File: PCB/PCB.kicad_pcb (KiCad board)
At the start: 4 copper layers, 56 x 55 mm, 15 parts, among them P1 SEN-11574, U1 TinyS3_Symbol, U2 ADXL345, U3 ST7789V, U4 switch3

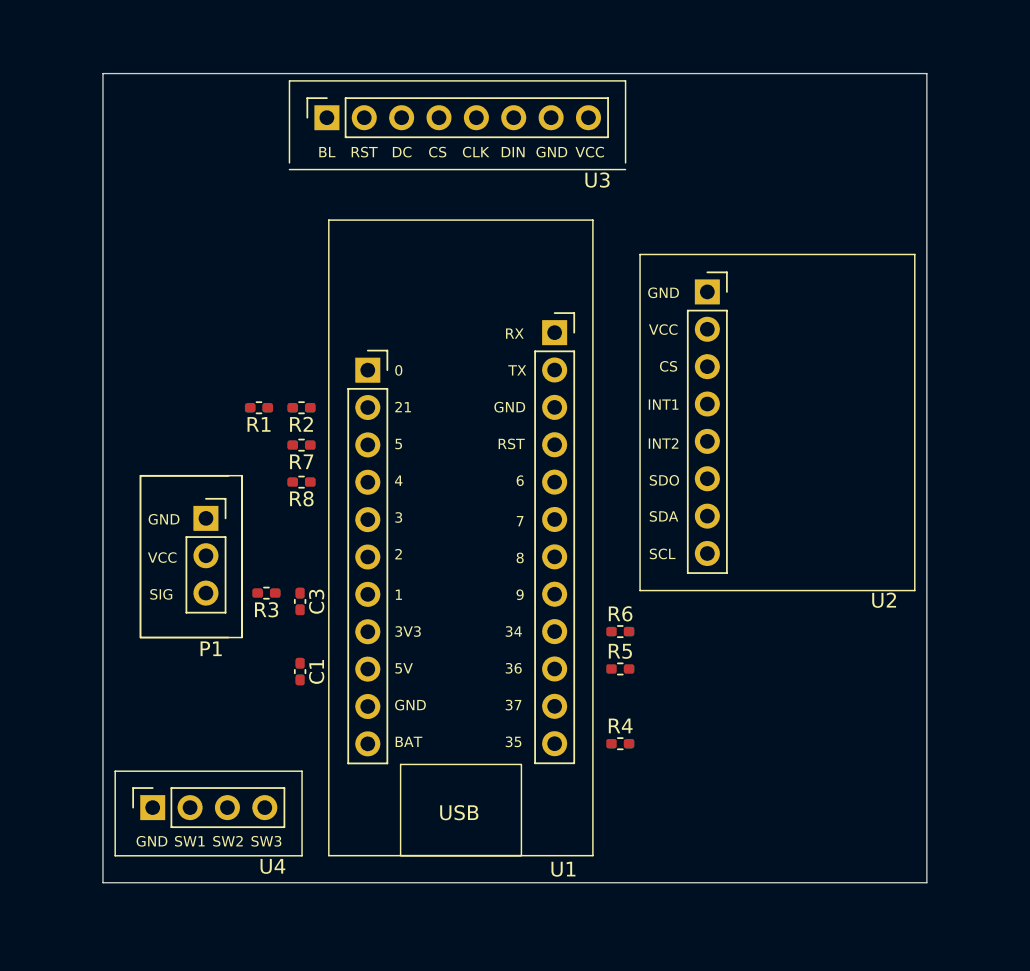
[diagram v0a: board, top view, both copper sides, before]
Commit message: PCB routed and DRC clean
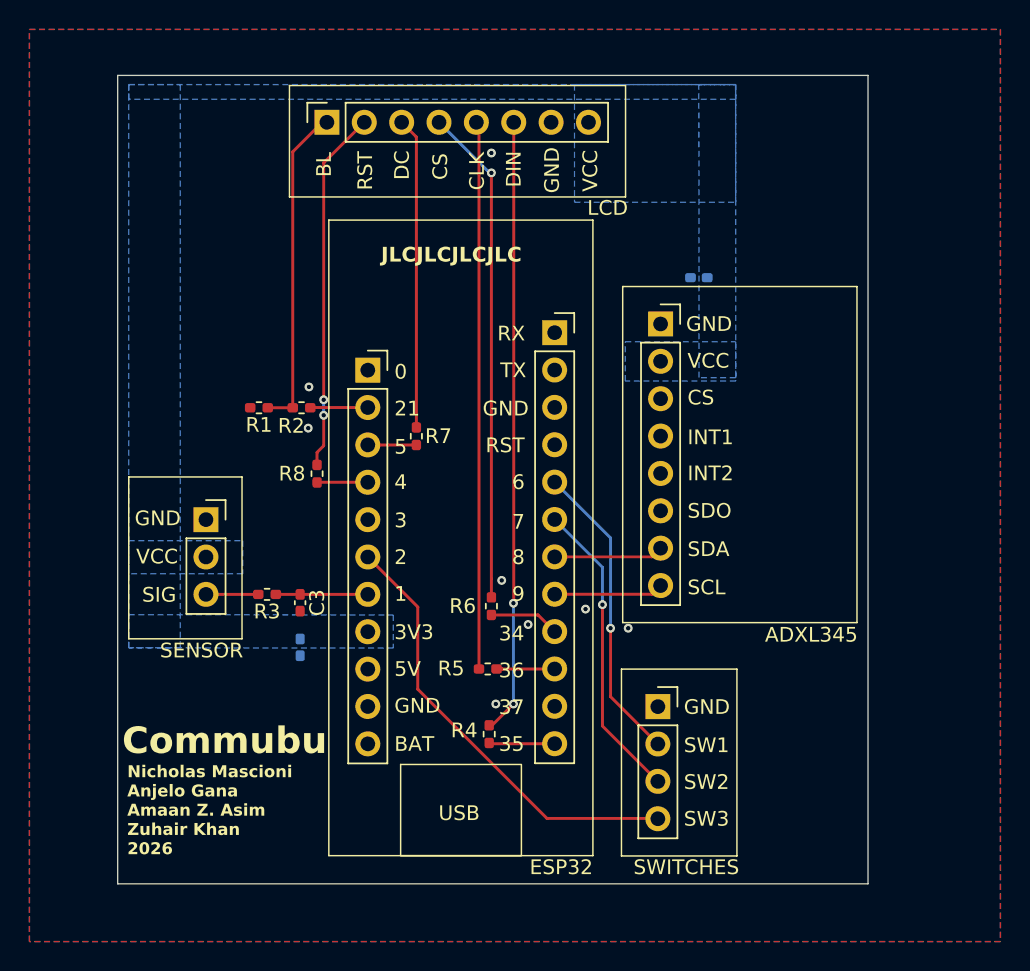
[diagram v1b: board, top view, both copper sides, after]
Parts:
- added C2: 10u, Capacitor_SMD:C_0402_1005Metric_Pad0.74x0.62mm_HandSolder, B.Cu at (150.5, 77.9)
- C1: moved to B.Cu
- moved SWITCHES 31.1 mm to (148.1, 110.4)
- moved R5 9.01 mm to (136.2, 104.5), turned to 180 degrees
- moved R4 8.93 mm to (136.2, 108.9), turned to 90 degrees
- moved R6 8.93 mm to (136.4, 100.2), turned to 90 degrees
- moved R7 7.83 mm to (131.3, 88.7), turned to 90 degrees
- moved ADXL345 3.85 mm to (147.9, 89.5)
- moved C1 1.65 mm to (123.4, 103.0)
- moved R8 1.20 mm to (124.5, 91.2), turned to 90 degrees
- moved LCD 0.31 mm to (134.1, 67.3)
- moved R3 0.10 mm to (121.2, 99.4)
- moved C3 0.09 mm to (123.4, 100.0)
- moved SENSOR 0.09 mm to (115.0, 96.9)
- renumbered U2 to ADXL345, U1 to ESP32, U3 to LCD, P1 to SENSOR, U4 to SWITCHES
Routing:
- net Net-(U3-DIN): track 0.00 -> 41.8 mm, vias 0 -> 2
- net Net-(U3-CLK): track 0.00 -> 37.5 mm
- net Net-(U3-CS): track 0.00 -> 33.8 mm, vias 0 -> 1
- net /BTN3: track 0.00 -> 30.7 mm
- net Net-(U3-RST): track 0.00 -> 24.8 mm, vias 0 -> 2
- net Net-(U3-BL): track 0.00 -> 22.4 mm
- net Net-(U3-DC): track 0.00 -> 21.2 mm
- net /BTN1: track 0.00 -> 20.7 mm, vias 0 -> 1
- net /BTN2: track 0.00 -> 20.7 mm, vias 0 -> 1
- net /SCL: track 0.00 -> 7.44 mm
- net /SDA: track 0.00 -> 7.44 mm
- net /FILTER_OUT: track 0.00 -> 6.32 mm
- net /CS: track 0.00 -> 4.77 mm
- net /DIN: track 0.00 -> 4.71 mm
- net /CLK: track 0.00 -> 3.95 mm
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- added copper zone on B.Cu, net +3V3
- added copper zone on B.Cu, net GND
- added copper zone on F.Cu, net GND
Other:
- board size 56 x 55 mm -> 51 x 55 mm
- board text added: "Commubu"
- board text added: "JLCJLCJLCJLC"
- board text added: "Nicholas Mascioni Anjelo Gana Amaan Z. Asim Zuhair Khan 2026"

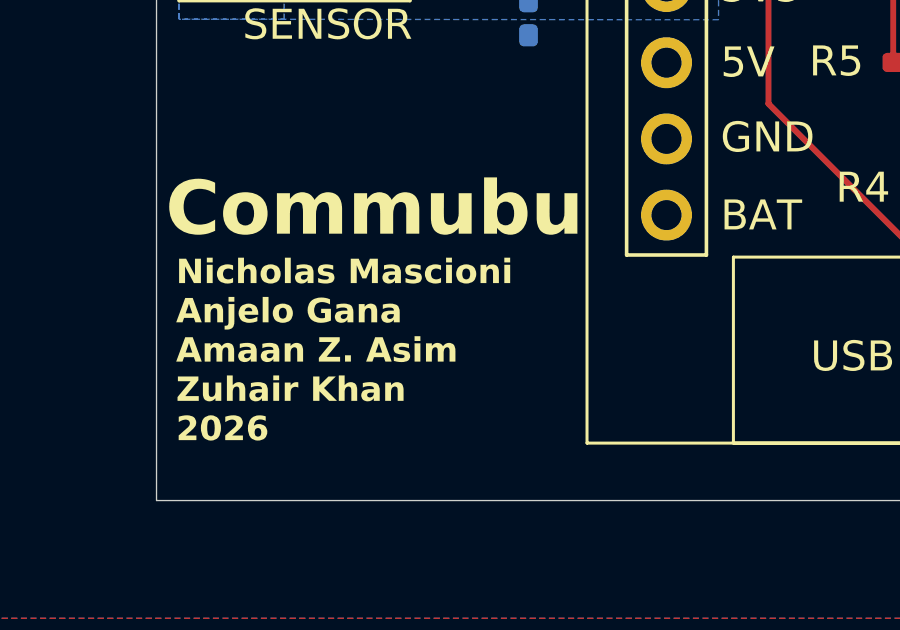
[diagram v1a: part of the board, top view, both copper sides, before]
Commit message: Added battery soldering pads
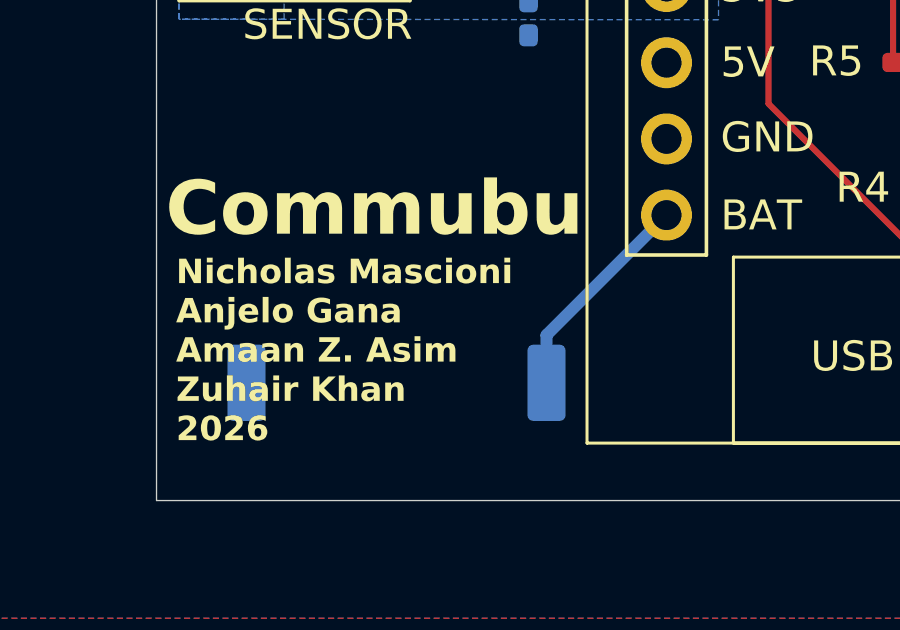
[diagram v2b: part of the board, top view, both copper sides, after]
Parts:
- added BATTERY: LiPO Pads, footprints:Battery_pads, B.Cu at (114.0, 115.2)
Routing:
- net +BATT: track 0.00 -> 7.25 mm

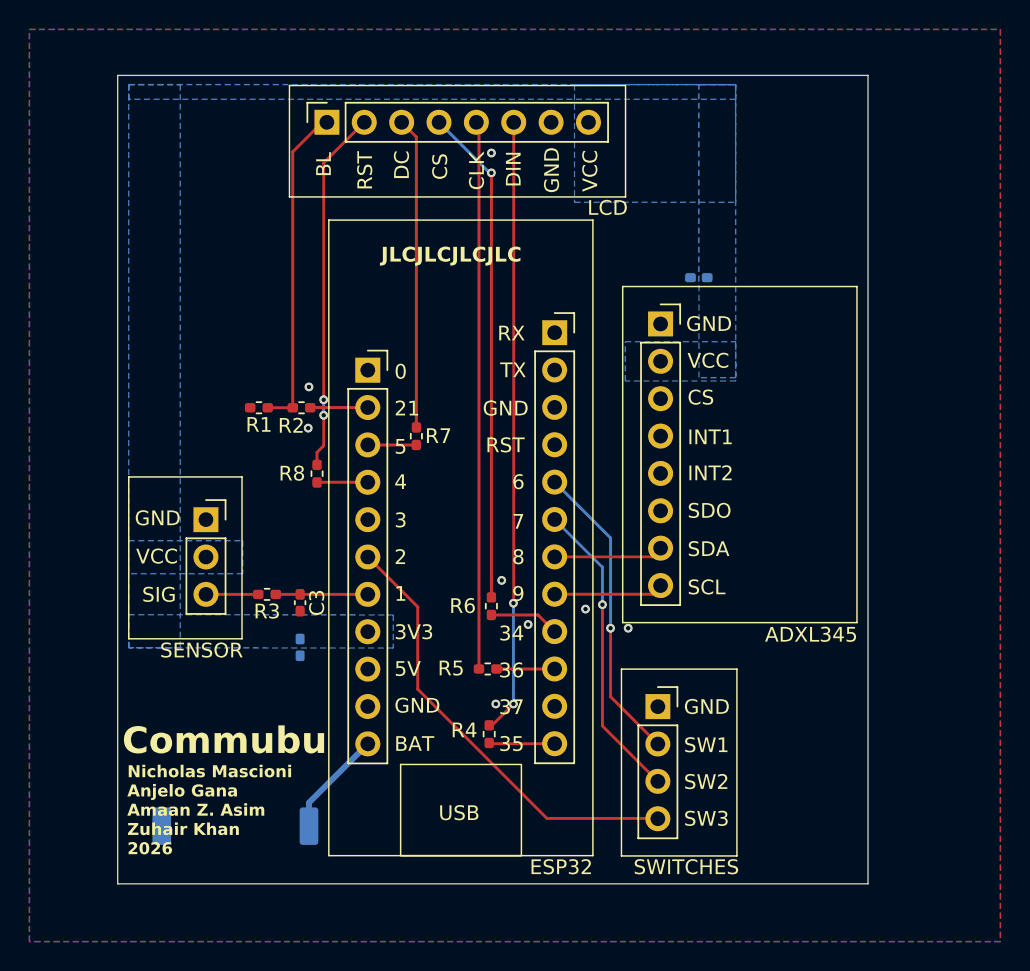
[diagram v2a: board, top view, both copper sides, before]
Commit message: Most recent PCB revisions, after fixing header width
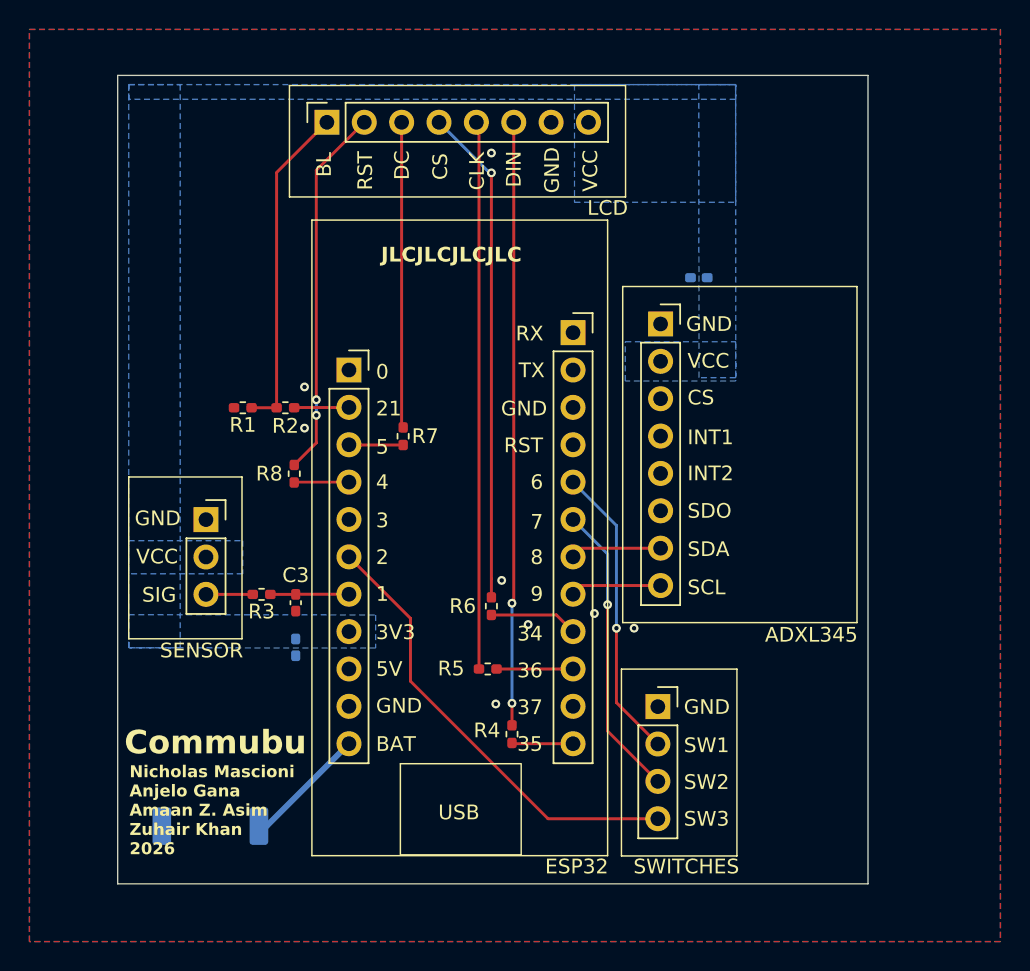
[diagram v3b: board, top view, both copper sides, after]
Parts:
- moved R4 1.55 mm to (137.8, 108.9)
- moved R8 1.55 mm to (123.0, 91.2)
- moved R1 1.10 mm to (119.5, 86.7)
- moved R2 1.10 mm to (122.4, 86.7)
- moved R7 0.90 mm to (130.4, 88.7)
- moved R3 0.38 mm to (120.8, 99.4)
- moved C1 0.30 mm to (123.1, 103.0)
- moved C3 0.30 mm to (123.1, 100.0)
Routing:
- net /CLK: track 3.95 -> 5.20 mm
- net /SDA: track 7.44 -> 6.19 mm
- net /SCL: track 7.44 -> 6.19 mm
- net /CS: track 4.77 -> 6.02 mm
- net +BATT: track 7.25 -> 8.44 mm
- net /FILTER_OUT: track 6.32 -> 5.35 mm
- net /DIN: track 4.71 -> 4.17 mm
- net /BTN1: track 20.7 -> 20.2 mm
- net /BTN2: track 20.7 -> 20.2 mm
